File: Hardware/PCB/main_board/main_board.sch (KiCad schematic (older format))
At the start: 17 parts

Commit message: Remove unused files
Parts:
- C1, C2, C3, C4: renamed from C?; footprint (none) -> Capacitor_SMD:C_0805_2012Metric
- R1, R2, R3, R4, R5, R6, R7: renamed from R?; footprint (none) -> Resistor_SMD:R_0805_2012Metric
- RV1, RV2: renamed from RV?; footprint (none) -> Potentiometer_THT:Potentiometer_Alps_RK09K_Single_Vertical
- U1: renamed from U?; footprint (none) -> Package_SO:SOIC-8_3.9x4.9mm_P1.27mm
- gave numbers to parts that had none: 1
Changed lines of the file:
@@
 $EndDescr
 $Comp
-L Amplifier_Operational:MCP6002-xSN U?
+L Amplifier_Operational:MCP6002-xSN U1
 U 1 1 5E4F00A7
 P 3550 2400
-F 0 "U?" H 3700 2500 50  0000 C CNN
+F 0 "U1" H 3700 2500 50  0000 C CNN
 F 1 "MCP6002-xSN" H 3750 2600 50  0000 C CNN
-F 2 "" H 3550 2400 50  0001 C CNN
+F 2 "Package_SO:SOIC-8_3.9x4.9mm_P1.27mm" H 3550 2400 50  0001 C CNN
 F 3 "http://ww1.microchip.com/downloads/en/DeviceDoc/21733j.pdf" H 3550 2400 50  0001 C CNN
 	1    3550 2400
@@
 $EndComp
 $Comp
-L Amplifier_Operational:MCP6002-xSN U?
+L Amplifier_Operational:MCP6002-xSN U1
 U 2 1 5E4F167C
 P 3350 4450
-F 0 "U?" H 3350 4817 50  0000 C CNN
+F 0 "U1" H 3350 4817 50  0000 C CNN
 F 1 "MCP6002-xSN" H 3350 4726 50  0000 C CNN
-F 2 "" H 3350 4450 50  0001 C CNN
+F 2 "Package_SO:SOIC-8_3.9x4.9mm_P1.27mm" H 3350 4450 50  0001 C CNN
 F 3 "http://ww1.microchip.com/downloads/en/DeviceDoc/21733j.pdf" H 3350 4450 50  0001 C CNN
 	2    3350 4450
@@
 $EndComp
 $Comp
-L Amplifier_Operational:MCP6002-xSN U?
+L Amplifier_Operational:MCP6002-xSN U1
 U 3 1 5E4F25DF
 P 3550 2400
-F 0 "U?" H 3508 2400 50  0001 L CNN
+F 0 "U1" H 3508 2400 50  0001 L CNN
 F 1 "MCP6002-xSN" H 3508 2355 50  0001 L CNN
-F 2 "" H 3550 2400 50  0001 C CNN
+F 2 "Package_SO:SOIC-8_3.9x4.9mm_P1.27mm" H 3550 2400 50  0001 C CNN
 F 3 "http://ww1.microchip.com/downloads/en/DeviceDoc/21733j.pdf" H 3550 2400 50  0001 C CNN
 	3    3550 2400
@@
 $EndComp
 $Comp
-L power:GND #PWR?
+L power:GND #PWR08
 U 1 1 5E4F8294
 P 3450 2700
-F 0 "#PWR?" H 3450 2450 50  0001 C CNN
+F 0 "#PWR08" H 3450 2450 50  0001 C CNN
 F 1 "GND" H 3455 2527 50  0000 C CNN
 F 2 "" H 3450 2700 50  0001 C CNN
@@
 $EndComp
 $Comp
-L power:+5VA #PWR?
+L power:+5VA #PWR07
 U 1 1 5E4F8A5C
 P 3450 2100
-F 0 "#PWR?" H 3450 1950 50  0001 C CNN
+F 0 "#PWR07" H 3450 1950 50  0001 C CNN
 F 1 "+5VA" H 3465 2273 50  0000 C CNN
 F 2 "" H 3450 2100 50  0001 C CNN
@@
 $EndComp
 $Comp
-L Device:R R?
+L Device:R R6
 U 1 1 5E4F9329
 P 3150 2750
-F 0 "R?" H 3220 2796 50  0000 L CNN
+F 0 "R6" H 3220 2796 50  0000 L CNN
 F 1 "100k" H 3220 2705 50  0000 L CNN
-F 2 "" V 3080 2750 50  0001 C CNN
+F 2 "Resistor_SMD:R_0805_2012Metric" V 3080 2750 50  0001 C CNN
 F 3 "~" H 3150 2750 50  0001 C CNN
 	1    3150 2750
@@
 $EndComp
 $Comp
-L power:+5VA #PWR?
+L power:+5VA #PWR04
 U 1 1 5E4FA16E
 P 2700 2500
-F 0 "#PWR?" H 2700 2350 50  0001 C CNN
+F 0 "#PWR04" H 2700 2350 50  0001 C CNN
 F 1 "+5VA" V 2715 2627 50  0000 L CNN
 F 2 "" H 2700 2500 50  0001 C CNN
@@
 $EndComp
 $Comp
-L power:GND #PWR?
+L power:GND #PWR06
 U 1 1 5E4FA400
 P 3150 2950
-F 0 "#PWR?" H 3150 2700 50  0001 C CNN
+F 0 "#PWR06" H 3150 2700 50  0001 C CNN
 F 1 "GND" H 3155 2777 50  0000 C CNN
 F 2 "" H 3150 2950 50  0001 C CNN
@@
 $EndComp
 $Comp
-L Device:R R?
+L Device:R R4
 U 1 1 5E4FA6CE
 P 2900 2300
-F 0 "R?" V 2693 2300 50  0000 C CNN
+F 0 "R4" V 2693 2300 50  0000 C CNN
 F 1 "1M" V 2784 2300 50  0000 C CNN
-F 2 "" V 2830 2300 50  0001 C CNN
+F 2 "Resistor_SMD:R_0805_2012Metric" V 2830 2300 50  0001 C CNN
 F 3 "~" H 2900 2300 50  0001 C CNN
 	1    2900 2300
@@
 $EndComp
 $Comp
-L Device:R R?
+L Device:R R5
 U 1 1 5E4F9D91
 P 2900 2500
-F 0 "R?" V 3000 2500 50  0000 C CNN
+F 0 "R5" V 3000 2500 50  0000 C CNN
 F 1 "100k" V 3100 2500 50  0000 C CNN
-F 2 "" V 2830 2500 50  0001 C CNN
+F 2 "Resistor_SMD:R_0805_2012Metric" V 2830 2500 50  0001 C CNN
 F 3 "~" H 2900 2500 50  0001 C CNN
 	1    2900 2500
@@
 $EndComp
 $Comp
-L Device:R R?
+L Device:R R3
 U 1 1 5E4FB4A7
 P 2100 2500
-F 0 "R?" H 2030 2454 50  0000 R CNN
+F 0 "R3" H 2030 2454 50  0000 R CNN
 F 1 "100k" H 2030 2545 50  0000 R CNN
-F 2 "" V 2030 2500 50  0001 C CNN
+F 2 "Resistor_SMD:R_0805_2012Metric" V 2030 2500 50  0001 C CNN
 F 3 "~" H 2100 2500 50  0001 C CNN
 	1    2100 2500
@@
 $EndComp
 $Comp
-L power:GND #PWR?
+L power:GND #PWR03
 U 1 1 5E4FB772
 P 2100 2700
-F 0 "#PWR?" H 2100 2450 50  0001 C CNN
+F 0 "#PWR03" H 2100 2450 50  0001 C CNN
 F 1 "GND" H 2105 2527 50  0000 C CNN
 F 2 "" H 2100 2700 50  0001 C CNN
@@
 $EndComp
 $Comp
-L Device:R R?
+L Device:R R7
 U 1 1 5E4FB9B1
 P 3500 1700
-F 0 "R?" V 3293 1700 50  0000 C CNN
+F 0 "R7" V 3293 1700 50  0000 C CNN
 F 1 "470k" V 3384 1700 50  0000 C CNN
-F 2 "" V 3430 1700 50  0001 C CNN
+F 2 "Resistor_SMD:R_0805_2012Metric" V 3430 1700 50  0001 C CNN
 F 3 "~" H 3500 1700 50  0001 C CNN
 	1    3500 1700
@@
 $EndComp
 $Comp
-L Device:R R?
+L Device:R R1
 U 1 1 5E4FBB35
 P 2050 900
-F 0 "R?" V 1843 900 50  0000 C CNN
+F 0 "R1" V 1843 900 50  0000 C CNN
 F 1 "10k" V 1934 900 50  0000 C CNN
-F 2 "" V 1980 900 50  0001 C CNN
+F 2 "Resistor_SMD:R_0805_2012Metric" V 1980 900 50  0001 C CNN
 F 3 "~" H 2050 900 50  0001 C CNN
 	1    2050 900
@@
 $EndComp
 $Comp
-L Device:R R?
+L Device:R R2
 U 1 1 5E4FC079
 P 2050 1400
-F 0 "R?" V 2150 1400 50  0000 C CNN
+F 0 "R2" V 2150 1400 50  0000 C CNN
 F 1 "10k" V 2250 1400 50  0000 C CNN
-F 2 "" V 1980 1400 50  0001 C CNN
+F 2 "Resistor_SMD:R_0805_2012Metric" V 1980 1400 50  0001 C CNN
 F 3 "~" H 2050 1400 50  0001 C CNN
 	1    2050 1400
@@
 $EndComp
 $Comp
-L Transistor_BJT:BC547 Q?
+L Transistor_BJT:BC547 Q1
 U 1 1 5E4FC367
 P 2800 1400
-F 0 "Q?" H 2991 1446 50  0000 L CNN
+F 0 "Q1" H 2991 1446 50  0000 L CNN
 F 1 "BC547" H 2991 1355 50  0000 L CNN
 F 2 "Package_TO_SOT_THT:TO-92_Inline" H 3000 1325 50  0001 L CIN
@@
 $EndComp
 $Comp
-L power:GND #PWR?
+L power:GND #PWR05
 U 1 1 5E4FD033
 P 2900 1600
-F 0 "#PWR?" H 2900 1350 50  0001 C CNN
+F 0 "#PWR05" H 2900 1350 50  0001 C CNN
 F 1 "GND" H 2905 1427 50  0000 C CNN
 F 2 "" H 2900 1600 50  0001 C CNN
@@
 $EndComp
 $Comp
-L Device:C C?
+L Device:C C2
 U 1 1 5E4FD243
 P 3300 1200
-F 0 "C?" V 3048 1200 50  0000 C CNN
+F 0 "C2" V 3048 1200 50  0000 C CNN
 F 1 "10n" V 3139 1200 50  0000 C CNN
-F 2 "" H 3338 1050 50  0001 C CNN
+F 2 "Capacitor_SMD:C_0805_2012Metric" H 3338 1050 50  0001 C CNN
 F 3 "~" H 3300 1200 50  0001 C CNN
 	1    3300 1200
@@
 $EndComp
 $Comp
-L Device:C C?
+L Device:C C3
 U 1 1 5E4FDA8C
 P 3800 1200
-F 0 "C?" V 3548 1200 50  0000 C CNN
+F 0 "C3" V 3548 1200 50  0000 C CNN
 F 1 "10n" V 3639 1200 50  0000 C CNN
-F 2 "" H 3838 1050 50  0001 C CNN
+F 2 "Capacitor_SMD:C_0805_2012Metric" H 3838 1050 50  0001 C CNN
 F 3 "~" H 3800 1200 50  0001 C CNN
 	1    3800 1200
@@
 $EndComp
 $Comp
-L Device:C C?
+L Device:C C4
 U 1 1 5E4FDBB7
 P 4100 2400
-F 0 "C?" V 3848 2400 50  0000 C CNN
+F 0 "C4" V 3848 2400 50  0000 C CNN
 F 1 "4.7u" V 3939 2400 50  0000 C CNN
-F 2 "" H 4138 2250 50  0001 C CNN
+F 2 "Capacitor_SMD:C_0805_2012Metric" H 4138 2250 50  0001 C CNN
 F 3 "~" H 4100 2400 50  0001 C CNN
 	1    4100 2400
@@
 $EndComp
 $Comp
-L Device:C C?
+L Device:C C1
 U 1 1 5E4FDDCA
 P 1850 2300
-F 0 "C?" V 1598 2300 50  0000 C CNN
+F 0 "C1" V 1598 2300 50  0000 C CNN
 F 1 "4.7u" V 1689 2300 50  0000 C CNN
-F 2 "" H 1888 2150 50  0001 C CNN
+F 2 "Capacitor_SMD:C_0805_2012Metric" H 1888 2150 50  0001 C CNN
 F 3 "~" H 1850 2300 50  0001 C CNN
 	1    1850 2300
@@
 $EndComp
 $Comp
-L Device:R_POT RV?
+L Device:R_POT RV1
 U 1 1 5E4FF171
 P 1500 1400
-F 0 "RV?" H 1430 1446 50  0000 R CNN
+F 0 "RV1" H 1430 1446 50  0000 R CNN
 F 1 "10k" H 1430 1355 50  0000 R CNN
-F 2 "" H 1500 1400 50  0001 C CNN
+F 2 "Potentiometer_THT:Potentiometer_Alps_RK09K_Single_Vertical" H 1500 1400 50  0001 C CNN
 F 3 "~" H 1500 1400 50  0001 C CNN
 	1    1500 1400
@@
 $EndComp
 $Comp
-L power:GND #PWR?
+L power:GND #PWR02
 U 1 1 5E4FF8FA
 P 1500 1600
-F 0 "#PWR?" H 1500 1350 50  0001 C CNN
+F 0 "#PWR02" H 1500 1350 50  0001 C CNN
 F 1 "GND" H 1505 1427 50  0000 C CNN
 F 2 "" H 1500 1600 50  0001 C CNN
@@
 $EndComp
 $Comp
-L power:+5VA #PWR?
+L power:+5VA #PWR01
 U 1 1 5E4FFA16
 P 1500 1200
-F 0 "#PWR?" H 1500 1050 50  0001 C CNN
+F 0 "#PWR01" H 1500 1050 50  0001 C CNN
 F 1 "+5VA" H 1515 1373 50  0000 C CNN
 F 2 "" H 1500 1200 50  0001 C CNN
@@
 $EndComp
 $Comp
-L Device:R_POT RV?
+L Device:R_POT RV2
 U 1 1 5E50004D
 P 4250 1200
-F 0 "RV?" V 4135 1200 50  0000 C CNN
+F 0 "RV2" V 4135 1200 50  0000 C CNN
 F 1 "10k" V 4044 1200 50  0000 C CNN
-F 2 "" H 4250 1200 50  0001 C CNN
+F 2 "Potentiometer_THT:Potentiometer_Alps_RK09K_Single_Vertical" H 4250 1200 50  0001 C CNN
 F 3 "~" H 4250 1200 50  0001 C CNN
 	1    4250 1200

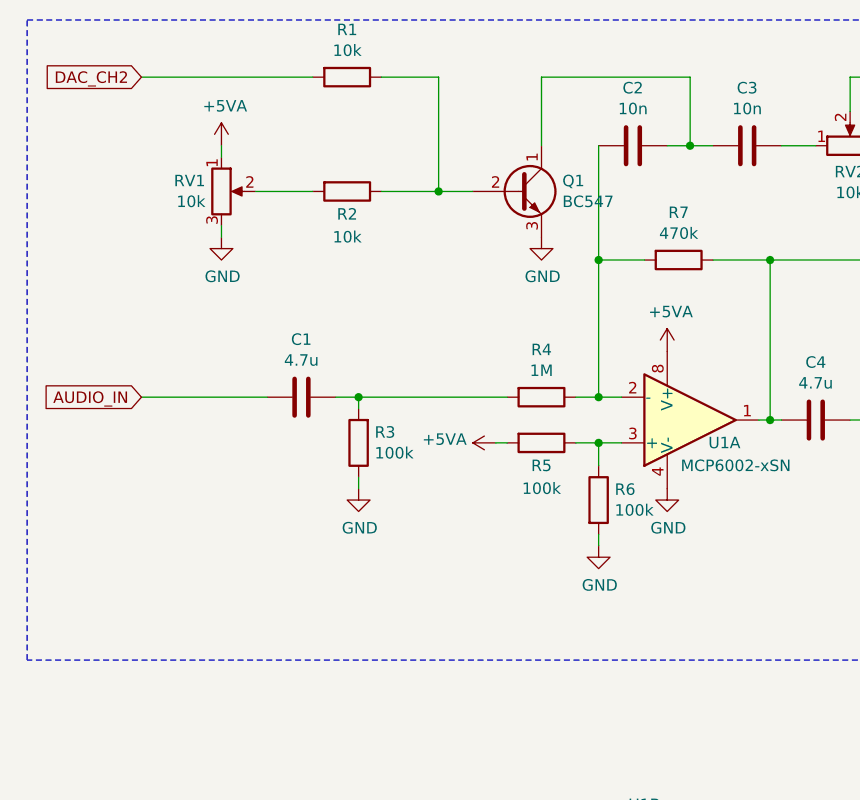
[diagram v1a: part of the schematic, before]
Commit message: Add PCB module for VCF
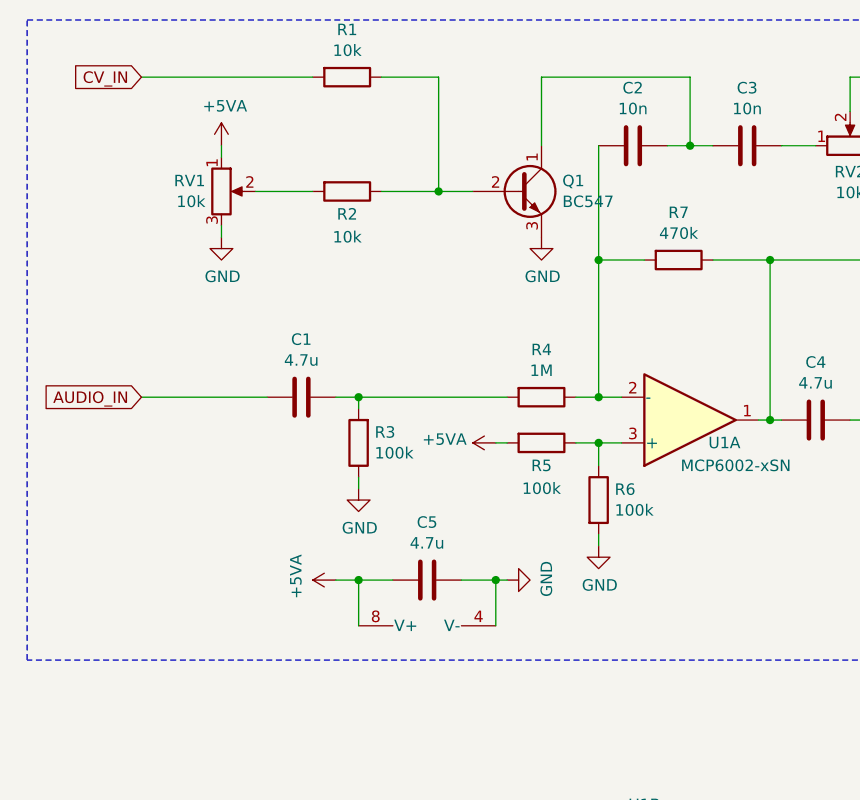
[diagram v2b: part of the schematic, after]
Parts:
- added C5: 4.7u, Capacitor_SMD:C_0805_2012Metric, symbol Device:C
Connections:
- net +5VA: now also C5.2
- net GND: now also C5.1
- net DAC_CH2 renamed CV_IN
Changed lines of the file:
@@
 L Amplifier_Operational:MCP6002-xSN U1
 U 3 1 5E4F25DF
-P 3550 2400
-F 0 "U1" H 3508 2400 50  0001 L CNN
-F 1 "MCP6002-xSN" H 3508 2355 50  0001 L CNN
-F 2 "Package_SO:SOIC-8_3.9x4.9mm_P1.27mm" H 3550 2400 50  0001 C CNN
-F 3 "http://ww1.microchip.com/downloads/en/DeviceDoc/21733j.pdf" H 3550 2400 50  0001 C CNN
-	3    3550 2400
-	1    0    0    -1
+P 2400 3200
+F 0 "U1" H 2358 3200 50  0001 L CNN
+F 1 "MCP6002-xSN" H 2358 3155 50  0001 L CNN
+F 2 "Package_SO:SOIC-8_3.9x4.9mm_P1.27mm" H 2400 3200 50  0001 C CNN
+F 3 "http://ww1.microchip.com/downloads/en/DeviceDoc/21733j.pdf" H 2400 3200 50  0001 C CNN
+	3    2400 3200
+	0    -1   -1   0
 $EndComp
 $Comp
 L power:GND #PWR08
 U 1 1 5E4F8294
-P 3450 2700
-F 0 "#PWR08" H 3450 2450 50  0001 C CNN
-F 1 "GND" H 3455 2527 50  0000 C CNN
-F 2 "" H 3450 2700 50  0001 C CNN
-F 3 "" H 3450 2700 50  0001 C CNN
-	1    3450 2700
-	1    0    0    -1
+P 2750 3100
+F 0 "#PWR08" H 2750 2850 50  0001 C CNN
+F 1 "GND" H 2755 2927 50  0000 C CNN
+F 2 "" H 2750 3100 50  0001 C CNN
+F 3 "" H 2750 3100 50  0001 C CNN
+	1    2750 3100
+	0    -1   -1   0
 $EndComp
 $Comp
 L power:+5VA #PWR07
 U 1 1 5E4F8A5C
-P 3450 2100
-F 0 "#PWR07" H 3450 1950 50  0001 C CNN
-F 1 "+5VA" H 3465 2273 50  0000 C CNN
-F 2 "" H 3450 2100 50  0001 C CNN
-F 3 "" H 3450 2100 50  0001 C CNN
-	1    3450 2100
-	1    0    0    -1
+P 2000 3100
+F 0 "#PWR07" H 2000 2950 50  0001 C CNN
+F 1 "+5VA" H 2015 3273 50  0000 C CNN
+F 2 "" H 2000 3100 50  0001 C CNN
+F 3 "" H 2000 3100 50  0001 C CNN
+	1    2000 3100
+	0    -1   -1   0
 $EndComp
 $Comp
@@
 	3150 2900 3150 2950
 Text GLabel 1150 900  0    50   Input ~ 0
-DAC_CH2
+CV_IN
 Text GLabel 1150 2300 0    50   Input ~ 0
 AUDIO_IN
@@
 Text Notes 4400 3400 0    118  ~ 24
 VCF\nlow pass
+$Comp
+L Device:C C5
+U 1 1 5E5083A9
+P 2400 3100
+F 0 "C5" V 2148 3100 50  0000 C CNN
+F 1 "4.7u" V 2239 3100 50  0000 C CNN
+F 2 "Capacitor_SMD:C_0805_2012Metric" H 2438 2950 50  0001 C CNN
+F 3 "~" H 2400 3100 50  0001 C CNN
+	1    2400 3100
+	0    1    1    0
+$EndComp
+Wire Wire Line
+	2100 3300 2100 3100
+Wire Wire Line
+	2100 3100 2000 3100
+Wire Wire Line
+	2250 3100 2100 3100
+Connection ~ 2100 3100
+Wire Wire Line
+	2550 3100 2700 3100
+Wire Wire Line
+	2700 3300 2700 3100
+Connection ~ 2700 3100
+Wire Wire Line
+	2700 3100 2750 3100
 $EndSCHEMATC

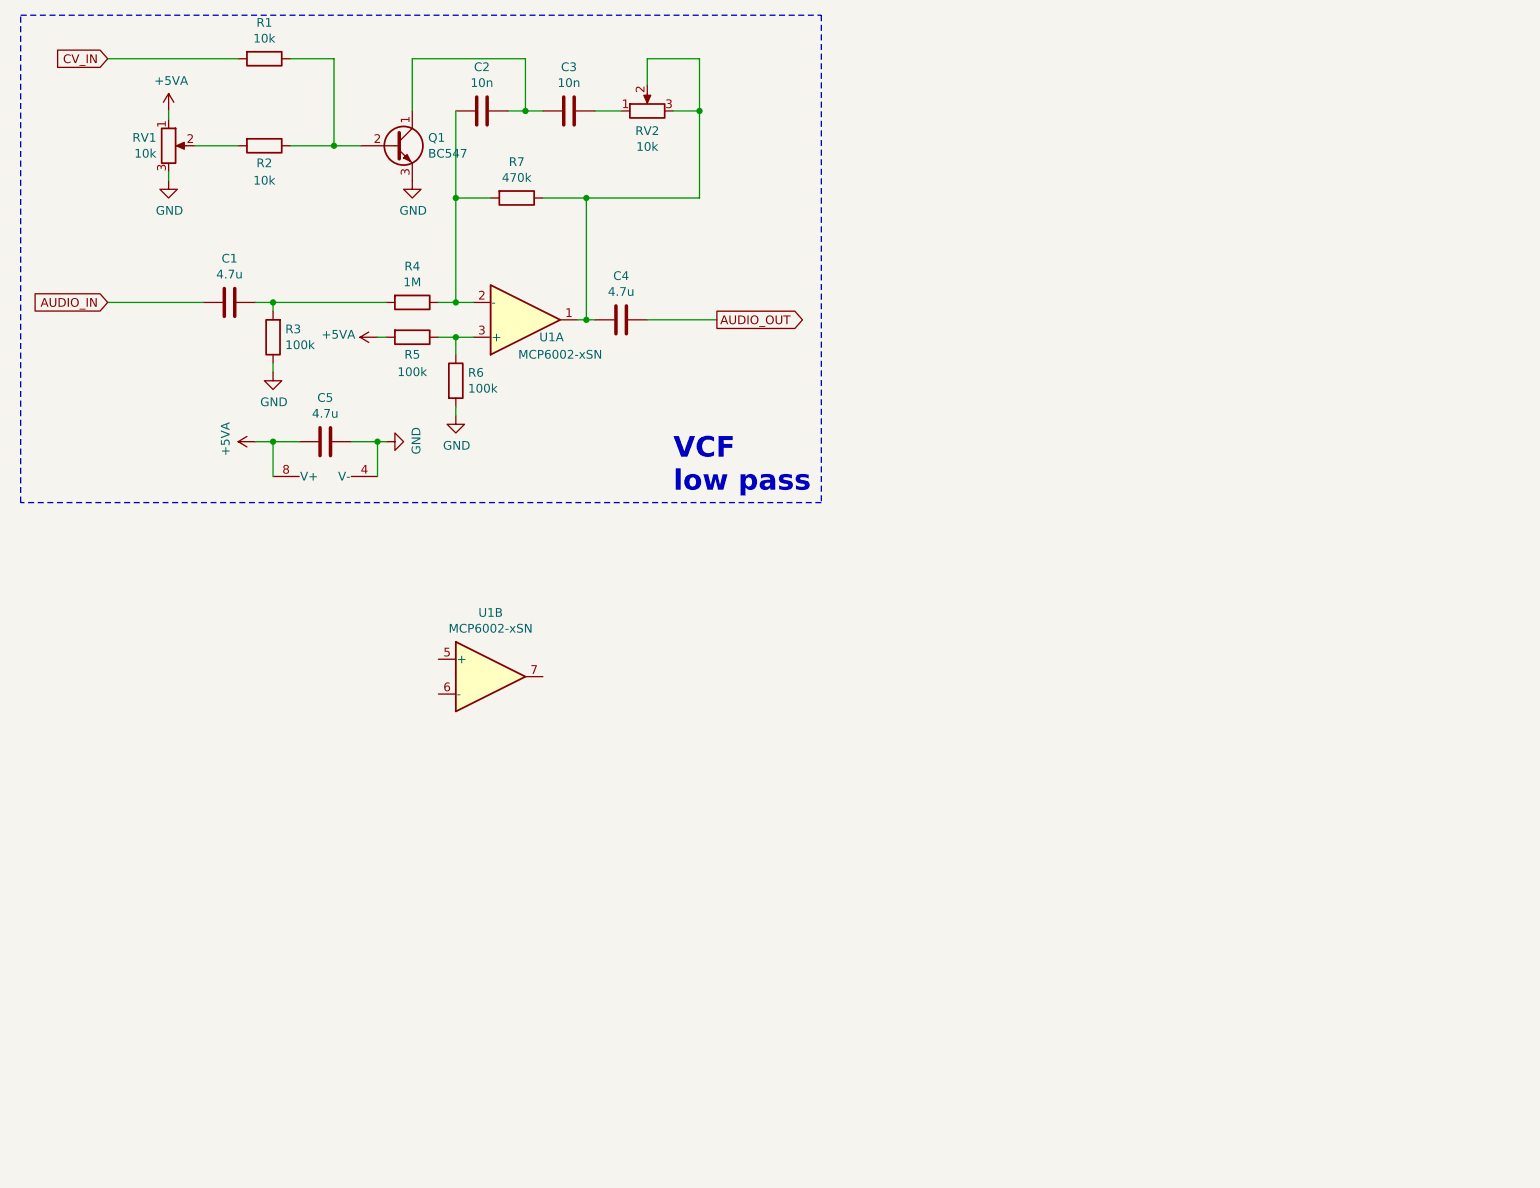
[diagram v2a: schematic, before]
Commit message: Add NUCLEO footprint
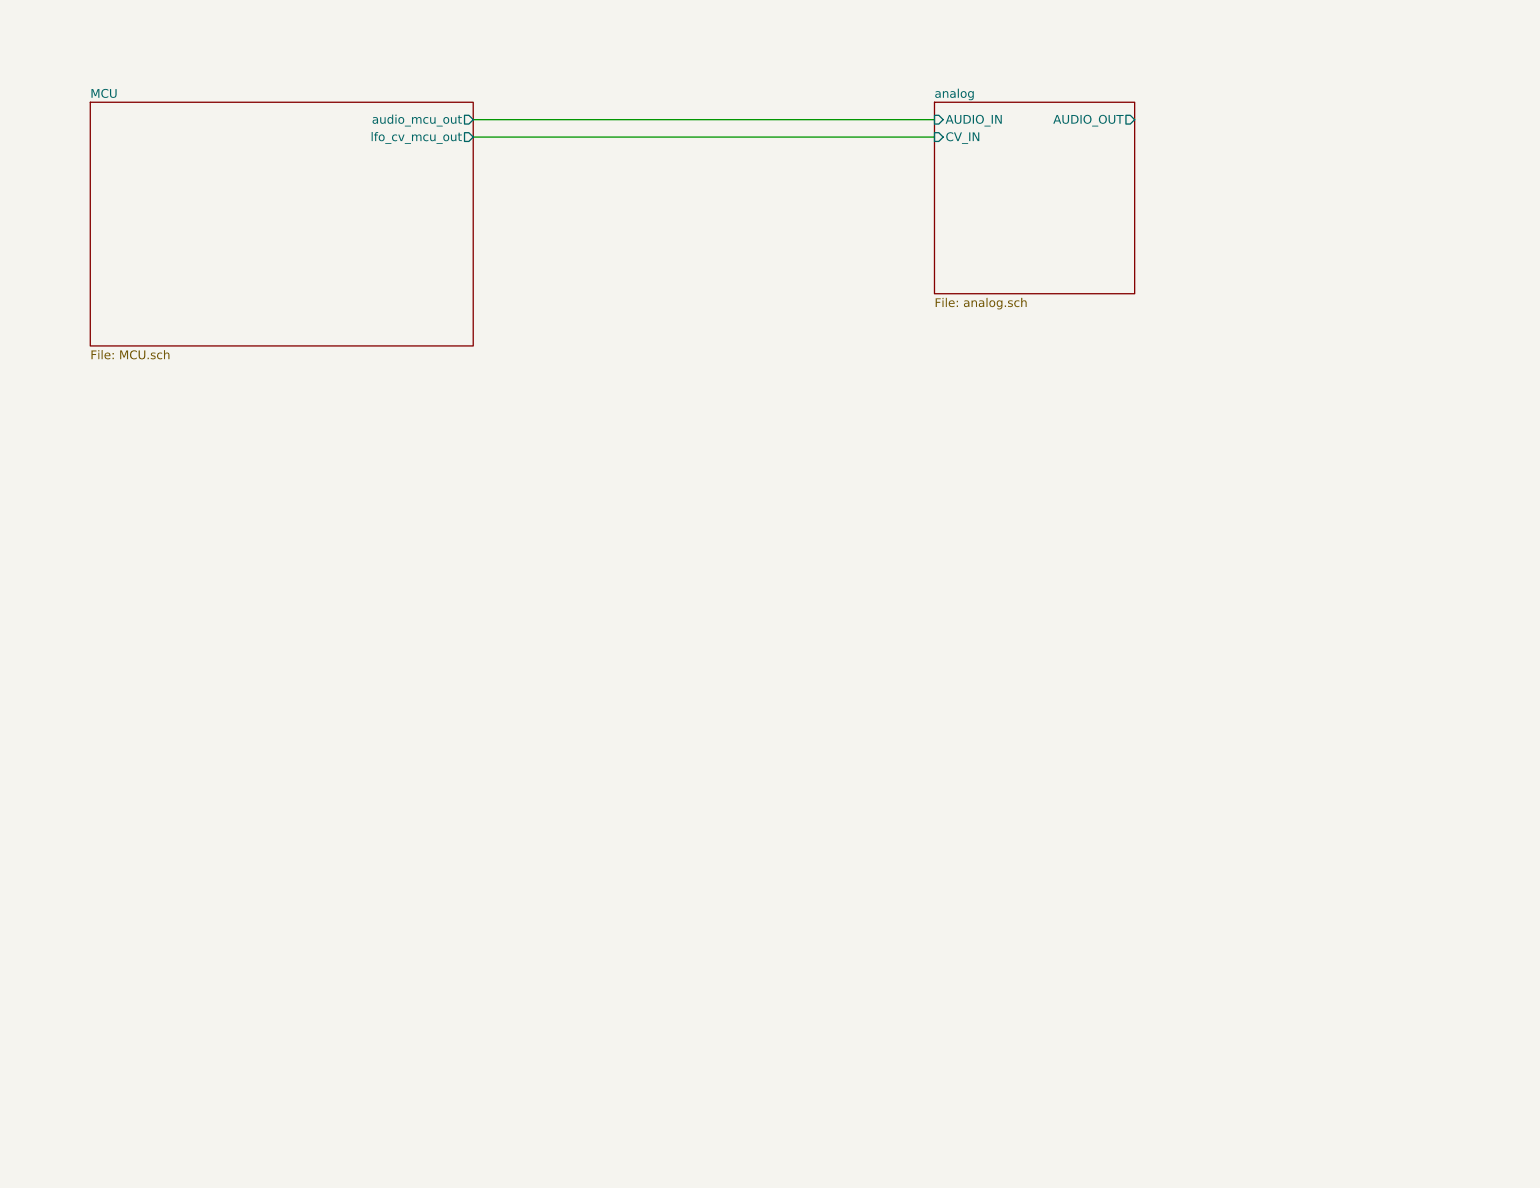
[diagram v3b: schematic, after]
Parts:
- removed C1, C4, C5: 4.7u, Capacitor_SMD:C_0805_2012Metric, symbol Device:C
- removed C2, C3: 10n, Capacitor_SMD:C_0805_2012Metric, symbol Device:C
- removed Q1: BC547, Package_TO_SOT_THT:TO-92_Inline, symbol Transistor_BJT:BC547
- removed R1, R2: 10k, Resistor_SMD:R_0805_2012Metric, symbol Device:R
- removed R3, R5, R6: 100k, Resistor_SMD:R_0805_2012Metric, symbol Device:R
- removed R4: 1M, Resistor_SMD:R_0805_2012Metric, symbol Device:R
- removed R7: 470k, Resistor_SMD:R_0805_2012Metric, symbol Device:R
- removed RV1, RV2: 10k, Potentiometer_THT:Potentiometer_Alps_RK09K_Single_Vertical, symbol Device:R_POT
- removed U1: MCP6002-xSN, Package_SO:SOIC-8_3.9x4.9mm_P1.27mm, symbol Amplifier_Operational:MCP6002-xSN
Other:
- note removed: "VCF\nlow pass"
